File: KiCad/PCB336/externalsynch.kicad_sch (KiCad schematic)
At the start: 15 parts, among them IC10 ADM4857ARZ-REEL7, IC11 ADM4857ARZ-REEL7, IC9 ISO6742FDWR, J5 105310-2210, J6 105310-2210

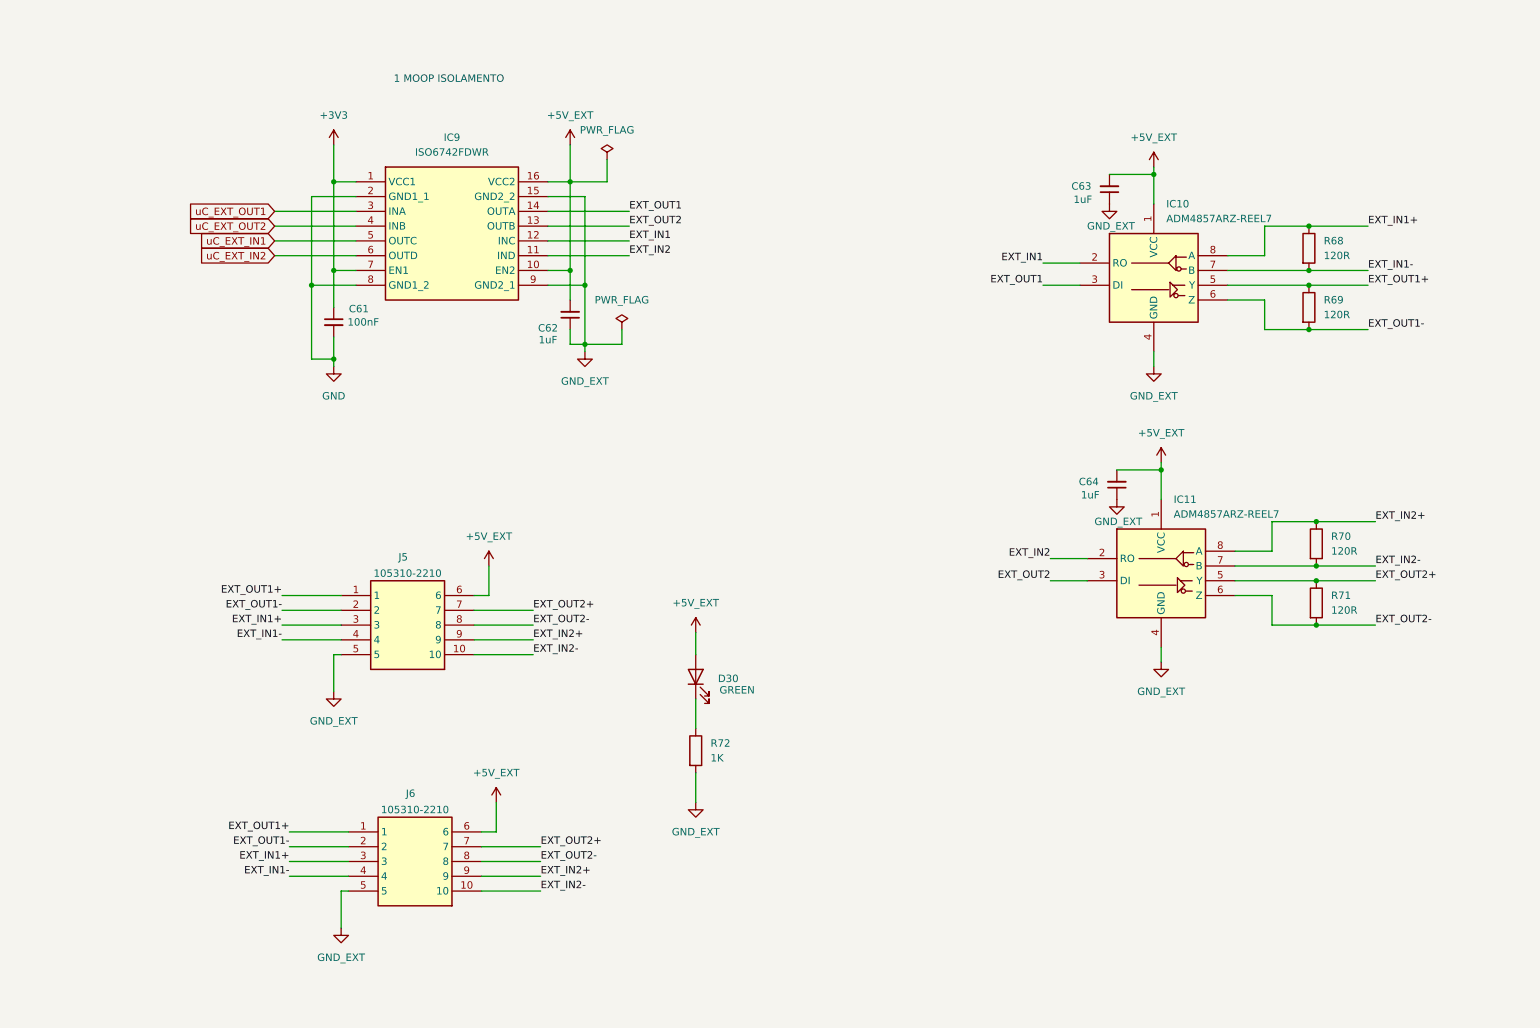
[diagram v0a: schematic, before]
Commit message: Iniziato loi sbroglio
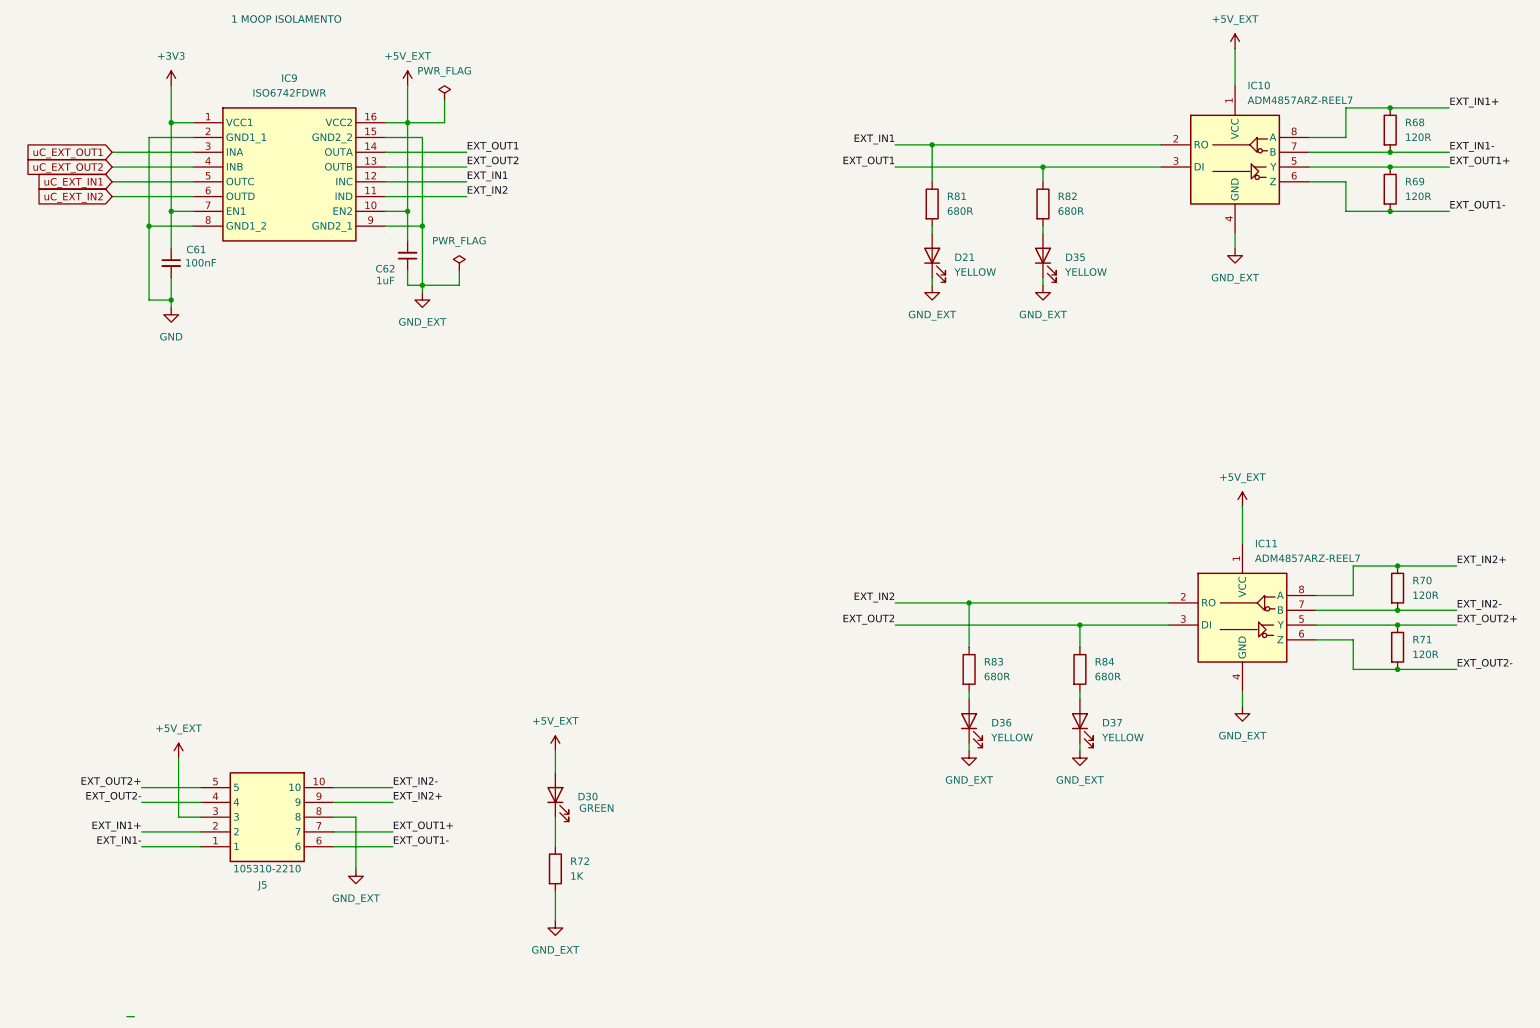
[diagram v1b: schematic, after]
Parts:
- removed C63, C64: 1uF, Capacitor_SMD:C_1206_3216Metric_Pad1.33x1.80mm_HandSolder, symbol Device:C_Small
- removed J6: 105310-2210, MET:1053102210, symbol MET:105310-2210
- added D21, D35, D36, D37: YELLOW, MET:LED_0805, symbol Device:LED
- added R81, R82, R83, R84: 680R, Resistor_SMD:R_0603_1608Metric_Pad0.98x0.95mm_HandSolder, symbol Device:R
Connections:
- net +5V_EXT: now also J5.3; no longer J5.6
- net EXT_IN1: now also R81.1
- net EXT_IN1+: now also J5.2; no longer J5.3
- net EXT_IN1-: now also J5.1; no longer J5.4
- net EXT_IN2: now also R83.1
- net EXT_OUT1: now also R82.1
- net EXT_OUT1+: now also J5.7; no longer J5.1
- net EXT_OUT1-: now also J5.6; no longer J5.2
- net EXT_OUT2: now also R84.1
- net EXT_OUT2+: now also J5.5; no longer J5.7
- net EXT_OUT2-: now also J5.4; no longer J5.8
- net GND_EXT: now also J5.8, D21.1 (K), D35.1 (K), D36.1 (K), D37.1 (K); no longer J5.5
- new net: D37.2 (A), R84.2
- new net: D21.2 (A), R81.2
- new net: D36.2 (A), R83.2
- new net: D35.2 (A), R82.2
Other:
- moved on the sheet: C61, C62, D30, IC10, IC11, IC9, R68, R69, R70, R71, R72
